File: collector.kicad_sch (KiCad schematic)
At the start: 2 parts, among them U14 CD74HCT32E

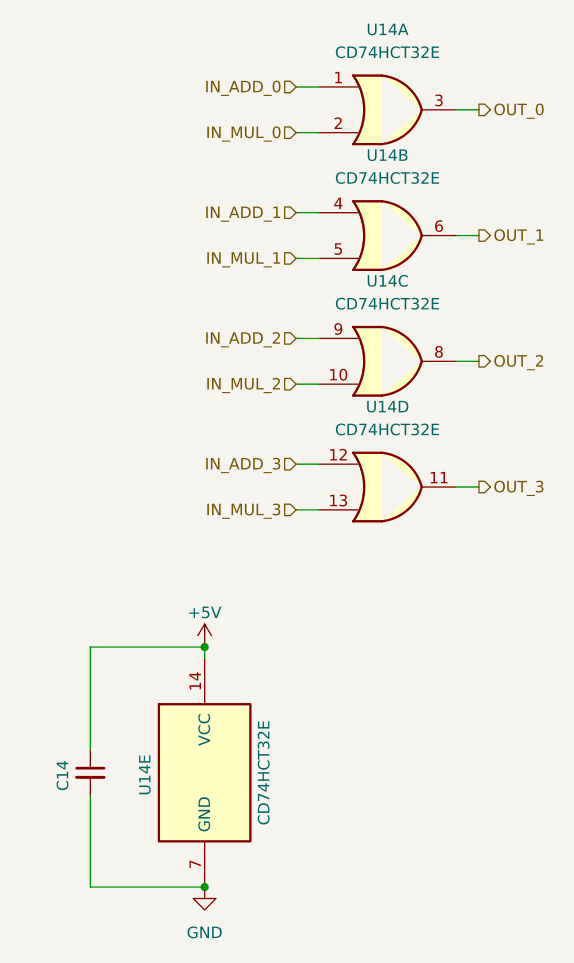
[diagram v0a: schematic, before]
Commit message: fix: change dip switch footprint
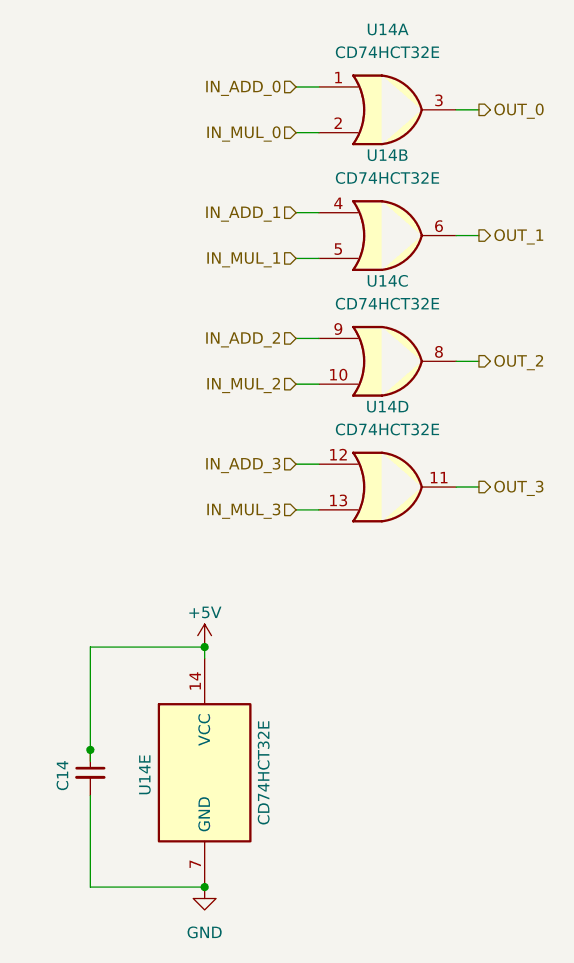
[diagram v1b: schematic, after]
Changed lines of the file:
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@@
 	(paper "A4")
+	(junction
+		(at 58.42 124.46)
+		(diameter 0)
+		(color 0 0 0 0)
+	)
 	(junction
 		(at 71.12 139.7)
@@
 		(pts
 			(xy 81.28 50.8) (xy 83.82 50.8)
+		)
+		(stroke
+			(width 0)
+			(type default)
+		)
+	)
+	(wire
+		(pts
+			(xy 58.42 124.46) (xy 58.42 113.03)
+		)
+		(stroke
+			(width 0)
+			(type default)
+		)
+	)
+	(wire
+		(pts
+			(xy 58.42 125.73) (xy 58.42 124.46)
 		)
 		(stroke
@@
 		)
 		(stroke
-			(width 0)
-			(type default)
-		)
-	)
-	(wire
-		(pts
-			(xy 58.42 113.03) (xy 58.42 124.46)
-		)
-		(stroke

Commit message: feat: updated references
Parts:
- C14: value C_Small -> CC0603KRX7R9BB104
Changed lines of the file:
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@@
 			)
 		)
-		(property "Value" "C_Small"
+		(property "Value" "CC0603KRX7R9BB104"
 			(at 60.96 128.2762 0)
 			(hide yes)

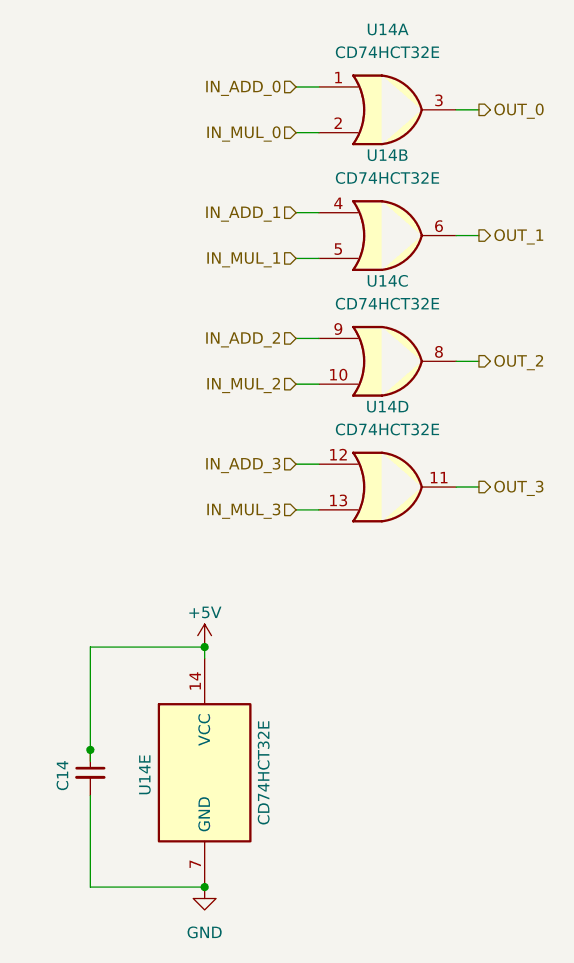
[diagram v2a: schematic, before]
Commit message: feat: pcb layout position
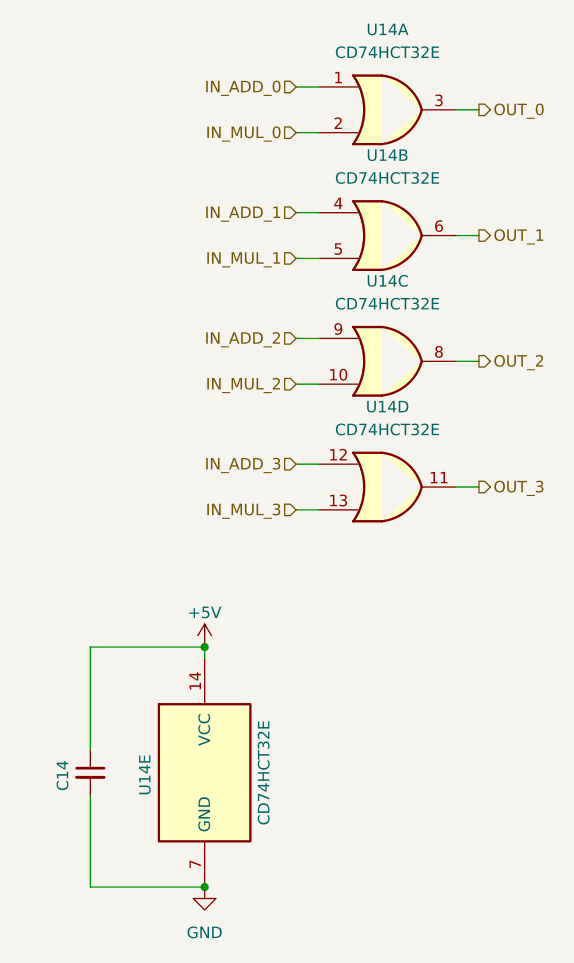
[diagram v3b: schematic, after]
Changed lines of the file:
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@@
 	(paper "A4")
-	(junction
-		(at 58.42 124.46)
-		(diameter 0)
-		(color 0 0 0 0)
-	)
 	(junction
 		(at 71.12 139.7)
@@
 		(pts
 			(xy 81.28 50.8) (xy 83.82 50.8)
-		)
-		(stroke
-			(width 0)
-			(type default)
-		)
-	)
-	(wire
-		(pts
-			(xy 58.42 124.46) (xy 58.42 113.03)
-		)
-		(stroke
-			(width 0)
-			(type default)
-		)
-	)
-	(wire
-		(pts
-			(xy 58.42 125.73) (xy 58.42 124.46)
 		)
 		(stroke
@@
 		)
 		(stroke
+			(width 0)
+			(type default)
+		)
+	)
+	(wire
+		(pts
+			(xy 58.42 113.03) (xy 58.42 124.46)
+		)
+		(stroke

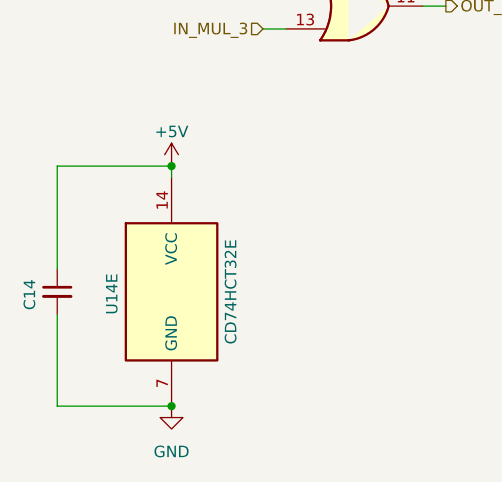
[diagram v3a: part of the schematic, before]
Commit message: Remove capacitors + change R and C footprints + finish PCB routing
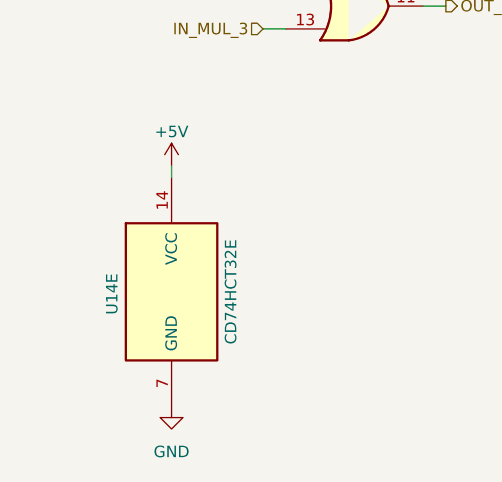
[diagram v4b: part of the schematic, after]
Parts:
- removed C14: CC0603KRX7R9BB104, Capacitor_SMD:C_0603_1608Metric_Pad1.08x0.95mm_HandSolder, symbol Device:C_Small
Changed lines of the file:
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@@
 	(generator_version "10.0")
 	(paper "A4")
-	(junction
-		(at 71.12 139.7)
-		(diameter 0)
-		(color 0 0 0 0)
-	)
-	(junction
-		(at 71.12 113.03)
-		(diameter 0)
-		(color 0 0 0 0)
-	)
 	(wire
 		(pts
@@
 	(wire
 		(pts
-			(xy 58.42 113.03) (xy 71.12 113.03)
-		)
-		(stroke
-			(width 0)
-			(type default)
-		)
-	)
-	(wire
-		(pts
 			(xy 81.28 83.82) (xy 83.82 83.82)
 		)
@@
 	(wire
 		(pts
-			(xy 58.42 139.7) (xy 71.12 139.7)
-		)
-		(stroke
-			(width 0)
-			(type default)
-		)
-	)
-	(wire
-		(pts
 			(xy 81.28 78.74) (xy 83.82 78.74)
 		)
@@
 		(pts
 			(xy 81.28 92.71) (xy 83.82 92.71)
-		)
-		(stroke
-			(width 0)
-			(type default)
-		)
-	)
-	(wire
-		(pts
-			(xy 58.42 129.54) (xy 58.42 139.7)
-		)
-		(stroke
-			(width 0)
-			(type default)
-		)
-	)
-	(wire
-		(pts
-			(xy 58.42 113.03) (xy 58.42 124.46)
 		)
 		(stroke
@@
 				)
 			)
-		)
-	)
-	(symbol
-		(lib_id "Device:C_Small")
-		(at 58.42 127 0)
-		(unit 1)
-		(body_style 1)
-		(exclude_from_sim no)
-		(in_bom yes)
-		(on_board yes)
-		(in_pos_files yes)
-		(dnp no)
-		(property "Reference" "C14"
-			(at 55.372 129.032 90)
-			(show_name no)
-			(do_not_autoplace no)
-			(effects
-				(font
-					(size 1.27 1.27)
-				)
-				(justify left)
-			)
-		)
-		(property "Value" "CC0603KRX7R9BB104"
-			(at 60.96 128.2762 0)
-			(hide yes)
-			(show_name no)
-			(do_not_autoplace no)
-			(effects
-				(font
-					(size 1.27 1.27)
-				)
-				(justify left)
-			)
-		)
-		(property "Footprint" "Capacitor_SMD:C_0603_1608Metric_Pad1.08x0.95mm_HandSolder"
-			(at 58.42 127 0)
-			(hide yes)
-			(show_name no)
-			(do_not_autoplace no)
-			(effects
-				(font
-					(size 1.27 1.27)
-				)
-			)
-		)
-		(property "Datasheet" ""
-			(at 58.42 127 0)
-			(hide yes)
-			(show_name no)
-			(do_not_autoplace no)
-			(effects
-				(font
-					(size 1.27 1.27)
-				)
-			)
-		)
-		(property "Description" "Unpolarized capacitor, small symbol"
-			(at 58.42 127 0)
-			(hide yes)
-			(show_name no)
-			(do_not_autoplace no)
-			(effects
-				(font
-					(size 1.27 1.27)
-				)
-			)
-		)
-		(pin "2"
-		)
-		(pin "1"
-		)
-		(instances
-			(project "alu"
-				(path "/4987240f-8890-46b8-b8e9-0d60580cb205/5c1c7519-ef63-46db-b588-8e7d91f6be11"
-					(reference "C14")
-					(unit 1)
-				)
-			)

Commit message: fix: reput capas -- where is my gift?
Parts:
- added C14: C_Small, Capacitor_SMD:C_0603_1608Metric, symbol Device:C_Small
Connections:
- net +5V: now also C14.1
- net GND: now also C14.2
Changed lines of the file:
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@@
 	(generator_version "9.0")
 	(paper "A4")
-	(wire
-		(pts (xy 81.28 50.8) (xy 83.82 50.8))
-		(stroke
-			(width 0)
-			(type default)
-		)
-	)
-	(wire
-		(pts (xy 81.28 83.82) (xy 83.82 83.82))
-		(stroke
-			(width 0)
-			(type default)
-		)
-	)
-	(wire
-		(pts (xy 99.06 53.34) (xy 101.6 53.34))
-		(stroke
-			(width 0)
-			(type default)
-		)
-	)
-	(wire
-		(pts (xy 81.28 78.74) (xy 83.82 78.74))
-		(stroke
-			(width 0)
-			(type default)
-		)
-	)
-	(wire
-		(pts (xy 99.06 67.31) (xy 101.6 67.31))
-		(stroke
-			(width 0)
-			(type default)
-		)
-	)
-	(wire
-		(pts (xy 99.06 95.25) (xy 101.6 95.25))
-		(stroke
-			(width 0)
-			(type default)
-		)
-	)
-	(wire
-		(pts (xy 81.28 97.79) (xy 83.82 97.79))
-		(stroke
-			(width 0)
-			(type default)
-		)
-	)
-	(wire
-		(pts (xy 99.06 81.28) (xy 101.6 81.28))
-		(stroke
-			(width 0)
-			(type default)
-		)
-	)
-	(wire
-		(pts (xy 81.28 92.71) (xy 83.82 92.71))
-		(stroke
-			(width 0)
-			(type default)
-		)
-	)
-	(wire
-		(pts (xy 71.12 113.03) (xy 71.12 114.3))
-		(stroke
-			(width 0)
-			(type default)
-		)
-	)
-	(wire
-		(pts (xy 81.28 64.77) (xy 83.82 64.77))
-		(stroke
-			(width 0)
-			(type default)
-		)
-	)
-	(wire
-		(pts (xy 81.28 69.85) (xy 83.82 69.85))
-		(stroke
-			(width 0)
-			(type default)
-		)
-	)
-	(wire
-		(pts (xy 81.28 55.88) (xy 83.82 55.88))
+	(junction
+		(at 71.12 114.3)
+		(diameter 0)
+		(color 0 0 0 0)
+	)
+	(junction
+		(at 71.12 139.7)
+		(diameter 0)
+		(color 0 0 0 0)
+	)
+	(wire
+		(pts
+			(xy 81.28 50.8) (xy 83.82 50.8)
+		)
+		(stroke
+			(width 0)
+			(type default)
+		)
+	)
+	(wire
+		(pts
+			(xy 81.28 83.82) (xy 83.82 83.82)
+		)
+		(stroke
+			(width 0)
+			(type default)
+		)
+	)
+	(wire
+		(pts
+			(xy 99.06 53.34) (xy 101.6 53.34)
+		)
+		(stroke
+			(width 0)
+			(type default)
+		)
+	)
+	(wire
+		(pts
+			(xy 81.28 78.74) (xy 83.82 78.74)
+		)
+		(stroke
+			(width 0)
+			(type default)
+		)
+	)
+	(wire
+		(pts
+			(xy 99.06 67.31) (xy 101.6 67.31)
+		)
+		(stroke
+			(width 0)
+			(type default)
+		)
+	)
+	(wire
+		(pts
+			(xy 99.06 95.25) (xy 101.6 95.25)
+		)
+		(stroke
+			(width 0)
+			(type default)
+		)
+	)
+	(wire
+		(pts
+			(xy 81.28 97.79) (xy 83.82 97.79)
+		)
+		(stroke
+			(width 0)
+			(type default)
+		)
+	)
+	(wire
+		(pts
+			(xy 99.06 81.28) (xy 101.6 81.28)
+		)
+		(stroke
+			(width 0)
+			(type default)
+		)
+	)
+	(wire
+		(pts
+			(xy 81.28 92.71) (xy 83.82 92.71)
+		)
+		(stroke
+			(width 0)
+			(type default)
+		)
+	)
+	(wire
+		(pts
+			(xy 52.07 128.27) (xy 52.07 139.7)
+		)
+		(stroke
+			(width 0)
+			(type default)
+		)
+	)
+	(wire
+		(pts
+			(xy 71.12 114.3) (xy 52.07 114.3)
+		)
+		(stroke
+			(width 0)
+			(type default)
+		)
+	)
+	(wire
+		(pts
+			(xy 52.07 139.7) (xy 71.12 139.7)
+		)
+		(stroke
+			(width 0)
+			(type default)
+		)
+	)
+	(wire
+		(pts
+			(xy 71.12 113.03) (xy 71.12 114.3)
+		)
+		(stroke
+			(width 0)
+			(type default)
+		)
+	)
+	(wire
+		(pts
+			(xy 81.28 64.77) (xy 83.82 64.77)
+		)
+		(stroke
+			(width 0)
+			(type default)
+		)
+	)
+	(wire
+		(pts
+			(xy 52.07 114.3) (xy 52.07 123.19)
+		)
+		(stroke
+			(width 0)
+			(type default)
+		)
+	)
+	(wire
+		(pts
+			(xy 81.28 69.85) (xy 83.82 69.85)
+		)
+		(stroke
+			(width 0)
+			(type default)
+		)
+	)
+	(wire
+		(pts
+			(xy 81.28 55.88) (xy 83.82 55.88)
+		)
 		(stroke
 			(width 0)
@@
 		(instances
 			(project "alu"
-				(path "/4987240f-8890-46b8-b8e9-0d60580cb205/5c1c7519-ef63-46db-b588-8e7d91f6be11" (reference "#PWR047") (unit 1))
+				(path "/4987240f-8890-46b8-b8e9-0d60580cb205/5c1c7519-ef63-46db-b588-8e7d91f6be11"
+					(reference "#PWR047")
+					(unit 1)
+				)
 			)
 		)
@@
 		(instances
 			(project "alu"
-				(path "/4987240f-8890-46b8-b8e9-0d60580cb205/5c1c7519-ef63-46db-b588-8e7d91f6be11" (reference "#PWR048") (unit 1))
+				(path "/4987240f-8890-46b8-b8e9-0d60580cb205/5c1c7519-ef63-46db-b588-8e7d91f6be11"
+					(reference "#PWR048")
+					(unit 1)
+				)
 			)
 		)
@@
 		(instances
 			(project "alu"
-				(path "/4987240f-8890-46b8-b8e9-0d60580cb205/5c1c7519-ef63-46db-b588-8e7d91f6be11" (reference "U14") (unit 4))
+				(path "/4987240f-8890-46b8-b8e9-0d60580cb205/5c1c7519-ef63-46db-b588-8e7d91f6be11"
+					(reference "U14")
+					(unit 4)
+				)
 			)
 		)
@@
 		(instances
 			(project "alu"
-				(path "/4987240f-8890-46b8-b8e9-0d60580cb205/5c1c7519-ef63-46db-b588-8e7d91f6be11" (reference "U14") (unit 5))
+				(path "/4987240f-8890-46b8-b8e9-0d60580cb205/5c1c7519-ef63-46db-b588-8e7d91f6be11"
+					(reference "U14")
+					(unit 5)
+				)
 			)
 		)
@@
 		(instances
 			(project "alu"
-				(path "/4987240f-8890-46b8-b8e9-0d60580cb205/5c1c7519-ef63-46db-b588-8e7d91f6be11" (reference "U14") (unit 3))
+				(path "/4987240f-8890-46b8-b8e9-0d60580cb205/5c1c7519-ef63-46db-b588-8e7d91f6be11"
+					(reference "U14")
+					(unit 3)
+				)
 			)
 		)
@@
 		(instances
 			(project "alu"
-				(path "/4987240f-8890-46b8-b8e9-0d60580cb205/5c1c7519-ef63-46db-b588-8e7d91f6be11" (reference "U14") (unit 1))
+				(path "/4987240f-8890-46b8-b8e9-0d60580cb205/5c1c7519-ef63-46db-b588-8e7d91f6be11"
+					(reference "U14")
+					(unit 1)
+				)
+			)
+		)
+	)
+	(symbol
+		(lib_id "Device:C_Small")
+		(at 52.07 125.73 0)
+		(unit 1)
+		(exclude_from_sim no)
+		(in_bom yes)
+		(on_board yes)
+		(dnp no)
+		(fields_autoplaced yes)
+		(property "Reference" "C14"
+			(at 54.61 124.4662 0)
+			(effects
+				(font
+					(size 1.27 1.27)
+				)
+				(justify left)
+			)
+		)
+		(property "Value" "C_Small"
+			(at 54.61 127.0062 0)
+			(effects
+				(font
+					(size 1.27 1.27)
+				)
+				(justify left)
+			)
+		)
+		(property "Footprint" "Capacitor_SMD:C_0603_1608Metric"
+			(at 52.07 125.73 0)
+			(effects
+				(font
+					(size 1.27 1.27)
+				)
+				(hide yes)
+			)
+		)
+		(property "Datasheet" "~"
+			(at 52.07 125.73 0)
+			(effects
+				(font
+					(size 1.27 1.27)
+				)
+				(hide yes)
+			)
+		)
+		(property "Description" "Unpolarized capacitor, small symbol"
+			(at 52.07 125.73 0)
+			(effects
+				(font
+					(size 1.27 1.27)
+				)
+				(hide yes)
+			)
+		)
+		(pin "2"
+		)
+		(pin "1"
+		)
+		(instances
+			(project "alu"
+				(path "/4987240f-8890-46b8-b8e9-0d60580cb205/5c1c7519-ef63-46db-b588-8e7d91f6be11"
+					(reference "C14")
+					(unit 1)
+				)
 			)
 		)
@@
 		(instances
 			(project "alu"
-				(path "/4987240f-8890-46b8-b8e9-0d60580cb205/5c1c7519-ef63-46db-b588-8e7d91f6be11" (reference "U14") (unit 2))
-			)
-		)
+				(path "/4987240f-8890-46b8-b8e9-0d60580cb205/5c1c7519-ef63-46db-b588-8e7d91f6be11"
+					(reference "U14")
+					(unit 2)
+				)
+			)
+		)
